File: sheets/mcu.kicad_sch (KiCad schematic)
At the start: 75 parts, among them J11 Conn_01x06, J12 Conn_01x02, J13 USB_B, J14 USB_B, J15 Conn_01x01, J16 Conn_01x01, J8 Conn_02x05_Odd_Even, J9 Conn_01x06, SW1 SW_Push, SW2 SW_Push, U23 REF3333, U24 LPS25HB, U25 XTSD04GLGEAG, U26 STM32H753ZIT6, U27 USBLC6-2SC6, U28 S3225SMD32.768KOSC, Y1 8MHz

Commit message: Remediate power supply, main relay keep-alive, and schematic ERC to 0 errors
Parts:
- removed C106: 100n, Capacitor_SMD:C_0603_1608Metric, symbol Device:C_Small
- removed U28: S3225SMD32.768KOSC, Package_TO_SOT_SMD:SOT-23-5, symbol Regulator_Linear:MIC5205-3.3YM5
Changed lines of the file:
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@@
 	)
 	(symbol
-		(lib_id "power:PWR_FLAG")
-		(at 91.44 247.65 90)
-		(unit 1)
-		(exclude_from_sim no)
-		(in_bom yes)
-		(on_board yes)
-		(dnp no)
-		(property "Reference" "#FLG07"
-			(at 89.535 247.65 0)
-			(effects
-				(font
-					(size 1.27 1.27)
-				)
-				(hide yes)
-			)
-		)
-		(property "Value" "PWR_FLAG"
-			(at 87.0458 247.65 0)
-			(effects
-				(font
-					(size 1.27 1.27)
-				)
-			)
-		)
-		(property "Footprint" ""
-			(at 91.44 247.65 0)
-			(effects
-				(font
-					(size 1.27 1.27)
-				)
-				(hide yes)
-			)
-		)
-		(property "Datasheet" "~"
-			(at 91.44 247.65 0)
-			(effects
-				(font
-					(size 1.27 1.27)
-				)
-				(hide yes)
-			)
-		)
-		(property "Description" ""
-			(at 91.44 247.65 0)
-			(effects
-				(font
-					(size 1.27 1.27)
-				)
-				(hide yes)
-			)
-		)
-		(pin "1"
-		)
-		(instances
-			(project "fome-mc"
-				(path "/3b9c5ffd-e59b-402d-8c5e-052f7ca643a4/00000000-0000-0000-0000-00005d99e6ee"
-					(reference "#FLG07")
-					(unit 1)
-				)
-			)
-		)
-	)
-	(symbol
-		(lib_id "power:PWR_FLAG")
-		(at 100.33 244.475 270)
-		(unit 1)
-		(exclude_from_sim no)
-		(in_bom yes)
-		(on_board yes)
-		(dnp no)
-		(property "Reference" "#FLG08"
-			(at 102.235 244.475 0)
-			(effects
-				(font
-					(size 1.27 1.27)
-				)
-				(hide yes)
-			)
-		)
-		(property "Value" "PWR_FLAG"
-			(at 104.7242 244.475 0)
-			(effects
-				(font
-					(size 1.27 1.27)
-				)
-			)
-		)
-		(property "Footprint" ""
-			(at 100.33 244.475 0)
-			(effects
-				(font
-					(size 1.27 1.27)
-				)
-				(hide yes)
-			)
-		)
-		(property "Datasheet" "~"
-			(at 100.33 244.475 0)
-			(effects
-				(font
-					(size 1.27 1.27)
-				)
-				(hide yes)
-			)
-		)
-		(property "Description" ""
-			(at 100.33 244.475 0)
-			(effects
-				(font
-					(size 1.27 1.27)
-				)
-				(hide yes)
-			)
-		)
-		(pin "1"
-		)
-		(instances
-			(project "fome-mc"
-				(path "/3b9c5ffd-e59b-402d-8c5e-052f7ca643a4/00000000-0000-0000-0000-00005d99e6ee"
-					(reference "#FLG08")
-					(unit 1)
-				)
-			)
-		)
-	)
-	(symbol
 		(lib_id "Connector_Generic:Conn_01x05")
 		(at 329.565 102.235 0)
@@
 		(effects (font (size 1.27 1.27)) (justify left bottom))
 	)
-	(symbol
-		(lib_id "Device:C_Small")
-		(at 235.0 44.45 0)
-		(unit 1)
-		(exclude_from_sim no)
-		(in_bom yes)
-		(on_board yes)
-		(dnp no)
-		(property "Reference" "C106"
-			(at 236.5 43.18 0)
-			(effects (font (size 1.27 1.27)) (justify left))
-		)
-		(property "Value" "100n"
-			(at 236.5 45.720000000000006 0)
-			(effects (font (size 1.27 1.27)) (justify left))
-		)
-		(property "Footprint" "Capacitor_SMD:C_0603_1608Metric"
-			(at 235.0 44.45 0)
-			(effects (font (size 1.27 1.27)) (hide yes))
-		)
-		(property "Datasheet" "~"
-			(at 235.0 44.45 0)
-			(effects (font (size 1.27 1.27)) (hide yes))
-		)
-		(property "LCSC" "C14663"
-			(at 235.0 44.45 0)
-			(effects (font (size 1.27 1.27)) (hide yes))
-		)
-		(pin "1")
-		(pin "2")
-		(instances
-			(project "fome-mc"
-				(path "/3b9c5ffd-e59b-402d-8c5e-052f7ca643a4/00000000-0000-0000-0000-00005d99e6ee"
-					(reference "C106")
-					(unit 1)
-				)
-			)
-		)
-	)
-	(symbol
-		(lib_id "Regulator_Linear:MIC5205-3.3YM5")
-		(at 235.0 34.29 0)
-		(unit 1)
-		(exclude_from_sim no)
-		(in_bom yes)
-		(on_board yes)
-		(dnp no)
-		(property "Reference" "U28"
-			(at 235.0 29.21 0)
-			(effects (font (size 1.27 1.27)))
-		)
-		(property "Value" "S3225SMD32.768KOSC"
-			(at 235.0 39.37 0)
-			(effects (font (size 1.27 1.27)))
-		)
-		(property "Footprint" "Package_TO_SOT_SMD:SOT-23-5"
-			(at 235.0 34.29 0)
-			(effects (font (size 1.27 1.27)) (hide yes))
-		)
-		(property "Datasheet" "~"
-			(at 235.0 34.29 0)
-			(effects (font (size 1.27 1.27)) (hide yes))
-		)
-		(property "LCSC" "C7431189"
-			(at 235.0 34.29 0)
-			(effects (font (size 1.27 1.27)) (hide yes))
-		)
-		(pin "1")
-		(pin "2")
-		(pin "3")
-		(pin "4")
-		(pin "5")
-		(instances
-			(project "fome-mc"
-				(path "/3b9c5ffd-e59b-402d-8c5e-052f7ca643a4/00000000-0000-0000-0000-00005d99e6ee"
-					(reference "U28")
-					(unit 1)
-				)
-			)
-		)
-	)
 	(hierarchical_label "BOOT0"

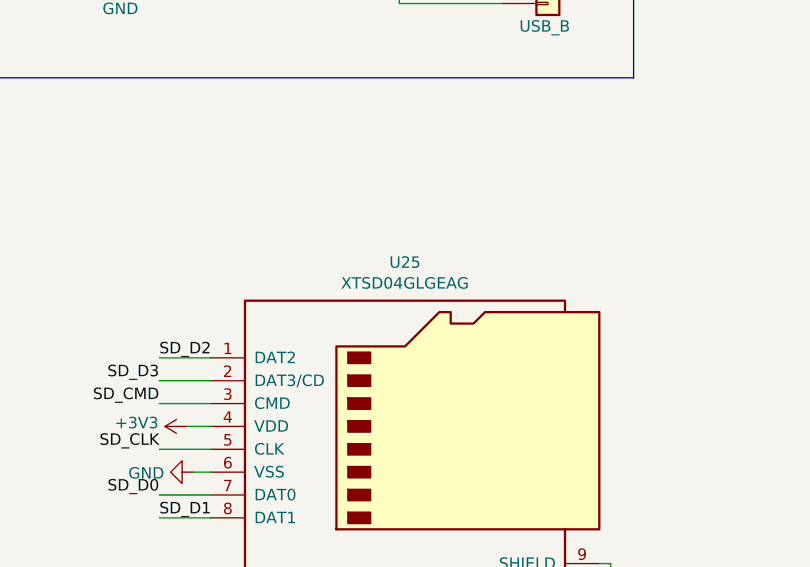
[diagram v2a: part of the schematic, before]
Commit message: FOMEMC-3: Upgrade U25 soldered SDNAND from 512 MB (4 Gbit) to 4 GB (32 Gbit CSNP32GCR01-AOW)
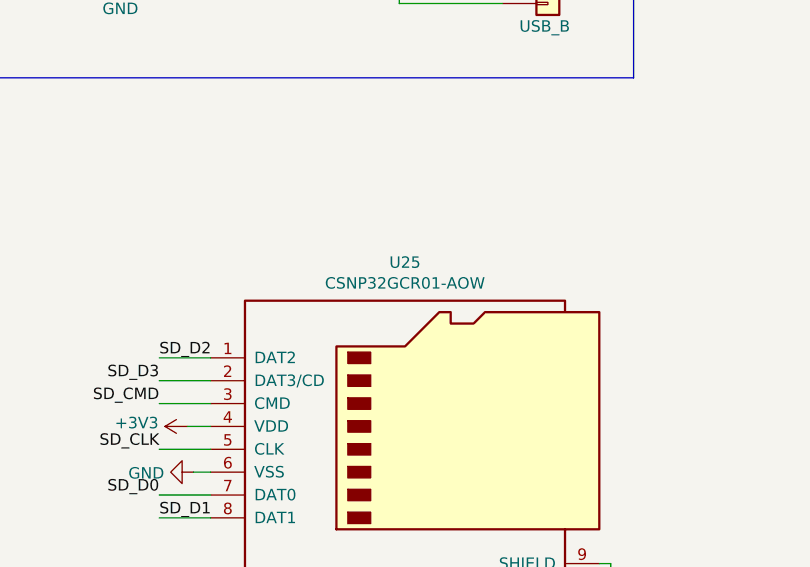
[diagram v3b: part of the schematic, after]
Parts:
- U25: value XTSD04GLGEAG -> CSNP32GCR01-AOW; LCSC C558840 -> C2841139; PN XTSD04GLGEAG -> CSNP32GCR01-AOW
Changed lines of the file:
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@@
 			)
 		)
-		(property "Value" "XTSD04GLGEAG"
+		(property "Value" "CSNP32GCR01-AOW"
 			(at 313.69 156.1846 0)
 			(effects
@@
 			)
 		)
-		(property "Datasheet" "https://datasheet.lcsc.com/lcsc/2005251034_XTX-XTSD04GLGEAG_C558840.pdf"
+		(property "Datasheet" "https://datasheet.lcsc.com/lcsc/2204261630_CS-CSNP32GCR01-AOW_C2841139.pdf"
 			(at 314.96 172.085 0)
 			(effects
@@
 			)
 		)
-		(property "Description" "4Gbit (512MB) Soldered Pottable SD NAND Flash LGA-8 6x8mm"
+		(property "Description" "32Gbit (4GB) Soldered Pottable SD NAND Flash LGA-8 6x8mm"
 			(at 314.96 172.085 0)
 			(effects
@@
 			)
 		)
-		(property "LCSC" "C558840"
+		(property "LCSC" "C2841139"
 			(at 314.96 172.085 0)
 			(effects
@@
 			)
 		)
-		(property "PN" "XTSD04GLGEAG"
+		(property "PN" "CSNP32GCR01-AOW"
 			(at 314.96 172.085 0)
 			(effects
@@
 			(project "fome-mc"
 				(path "/3b9c5ffd-e59b-402d-8c5e-052f7ca643a4/00000000-0000-0000-0000-00005d99e6ee"
-					(reference "U25")
-					(unit 1)
-				)
-			)
-			(project "fome-mc"
-				(path "/3b9c5ffd-e59b-402d-8c5e-052f7ca643a4/00000000-0000-0000-0000-00005d99e6ee"

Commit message: Re-integrate ATWINC1500-MR210UB Wi-Fi on SPI4 and remap WBO1/2 reset/boot pins (FOMEMC-2)
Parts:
- added C106: 100n, Capacitor_SMD:C_0603_1608Metric, symbol Device:C_Small
- added R122: 10k, Resistor_SMD:R_0402_1005Metric, symbol Device:R_Small
- added U29: ATWINC1500-MR210UB, ampseal:ATWINC1500-MR210UB, symbol RF_WiFi:ATWINC1500-MR210UB
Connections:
- net IGN12 is gone; now on net WBO1_NRST: U26.118 (PD4)
- net IGN9 is gone; now on net WBO2_BOOT0: U26.123 (PD7)
- net +3V3: now also C106.1, R122.1, U29.20 (VBAT), U29.23 (VDDIO)
- net GND: now also C106.2, U29.12 (GND_2), U29.28 (GND_3), U29.29 (EP), U29.9 (GND_1)
- net WBO1_BOOT0: now also U26.119 (PD5); no longer U26.2 (PE3)
- net WBO1_NRST: no longer U26.1 (PE2)
- net WBO2_BOOT0: no longer U26.4 (PE5)
- net WBO2_NRST: now also U26.122 (PD6); no longer U26.3 (PE4)
- net WIFI_MOSI: now reaches U26.5 (PE6)
- net WIFI_MOSI: now also U29.15 (SPI_RXD)
- net WIFI_RST: now reaches U26.7 (PC13)
- net WIFI_RST: now also U29.4 (RESET_N)
- net IGN10: no longer names the net of J12.2 (Pin_2)
- net IGN10: no longer U26.122 (PD6)
- net IGN11: no longer names the net of J12.1 (Pin_1)
- net IGN11: no longer U26.119 (PD5)
- new net WIFI_CS: U26.3 (PE4), U29.16 (SPI_SSN)
- new net WIFI_EN: R122.2, U29.10 (SPI_CFG), U29.11 (WAKE), U29.22 (CHIP_EN)
- new net WIFI_IRQ: U26.2 (PE3), U29.13 (IRQN)
- new net WIFI_MISO: U26.4 (PE5), U29.17 (SPI_TXD)
- new net WIFI_SCK: U26.1 (PE2), U29.18 (SPI_SCK)
- no-connect marks 18 -> 32

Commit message: Add SDMMC1 47k pull-ups (R127..R131) & 22R clock damping (R132), mark U24 LPS25HB DNP, fix B340A/B5819W LCSC codes, and reconcile docs/verify_io_map (FOMEMC-8)
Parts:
- added R127, R128, R129, R130, R131: 47k, Resistor_SMD:R_0402_1005Metric, symbol Device:R
- added R132: 22, Resistor_SMD:R_0603_1608Metric, symbol Device:R
- D14, D6, D7, D8: value schottky -> B5819W
- U24: now not fitted; now left out of the parts list
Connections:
- net +3V3: now also R127.1, R128.1, R129.1, R130.1, R131.1
- net SD_CLK: now also R132.1; no longer U25.5 (CLK)
- net SD_CMD: now also R131.2
- net SD_D0: now also R127.2
- net SD_D1: now also R128.2
- net SD_D2: now also R129.2
- net SD_D3: now also R130.2
- new net: R132.2, U25.5 (CLK)

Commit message: Synchronize PCB footprints, netlist pad assignments, DNP flags, and zone priorities with schematic (FOMEMC-9)
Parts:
- D10, D11, D12, D13, D9: footprint LED_SMD:LED_0603_1608Metric_Castellated -> LED_SMD:LED_0603_1608Metric
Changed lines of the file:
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@@
 			)
 		)
-		(property "Footprint" "LED_SMD:LED_0603_1608Metric_Castellated"
+		(property "Footprint" "LED_SMD:LED_0603_1608Metric"
 			(at 211.455 173.99 0)
 			(effects
@@
 			)
 		)
-		(property "Footprint" "LED_SMD:LED_0603_1608Metric_Castellated"
+		(property "Footprint" "LED_SMD:LED_0603_1608Metric"
 			(at 211.455 184.15 0)
 			(effects
@@
 			)
 		)
-		(property "Footprint" "LED_SMD:LED_0603_1608Metric_Castellated"
+		(property "Footprint" "LED_SMD:LED_0603_1608Metric"
 			(at 211.455 193.675 0)
 			(effects
@@
 			)
 		)
-		(property "Footprint" "LED_SMD:LED_0603_1608Metric_Castellated"
+		(property "Footprint" "LED_SMD:LED_0603_1608Metric"
 			(at 211.455 203.2 0)
 			(effects
@@
 			)
 		)
-		(property "Footprint" "LED_SMD:LED_0603_1608Metric_Castellated"
+		(property "Footprint" "LED_SMD:LED_0603_1608Metric"
 			(at 211.455 212.725 0)
 			(effects

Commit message: Remediate FOMEMC-17..20: 50V X7R PSU caps & 42V INJ clamp DNP, U29 DS70005304F footprint + 1P3V bypass, HV_IGN 0.50mm clearance + U25 decoupling, and 0 ERC violations
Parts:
- added C111: 10u, Capacitor_SMD:C_0603_1608Metric, symbol Device:C_Small
- added C112: 10n, Capacitor_SMD:C_0603_1608Metric, symbol Device:C_Small
- added C113: 4.7u, Capacitor_SMD:C_0603_1608Metric, symbol Device:C_Small
- added C114: 100n, Capacitor_SMD:C_0603_1608Metric, symbol Device:C_Small
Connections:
- net +3V3: now also C113.1, C114.1
- net GND: now also C111.2, C112.2, C113.2, C114.2
- net WIFI_1P3V: now reaches U29.24 (1P3V_TP)
- net WIFI_1P3V: now also C111.1, C112.1
- net LS10: no longer names the net of U26.135 (PB5)
- net LS11: no longer names the net of U26.136 (PB6)
- net LSE_32K: no longer names the net of U26.8 (PC14)
- net RC1: no longer names the net of U26.100 (PA8)
- net TRIGGER_SCOPE: no longer names the net of U26.22 (PF10)
- no-connect marks 32 -> 36

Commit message: Remediate FOMEMC-22..27: sheet contracts, doc/BOM/netlist parity, 494-part BOM/CPL, Mode A2 VR + C38/C39, wide WBO heater buses, and 4x M4 holes with 0 DRC warnings
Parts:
- BT1, J11, J12, J13, J14, J15, J16, J8, J9: now not fitted; now left out of the parts list
- C103, C104, C105, C106, C114, C61, C62, C63, C64, C67, C68, C69, C70, C71, C73, C79, C81, C83: LCSC C14663 -> C161115
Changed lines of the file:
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@@
 			)
 		)
-		(property "LCSC" "C14663"
+		(property "LCSC" "C161115"
 			(at 43.18 29.845 0)
 			(effects
@@
 			)
 		)
-		(property "LCSC" "C14663"
+		(property "LCSC" "C161115"
 			(at 48.26 29.845 0)
 			(effects
@@
 			)
 		)
-		(property "LCSC" "C14663"
+		(property "LCSC" "C161115"
 			(at 53.34 29.845 0)
 			(effects
@@
 			)
 		)
-		(property "LCSC" "C14663"
+		(property "LCSC" "C161115"
 			(at 58.42 29.845 0)
 			(effects
@@
 			)
 		)
-		(property "LCSC" "C14663"
+		(property "LCSC" "C161115"
 			(at 68.58 29.845 0)
 			(effects
@@
 			)
 		)
-		(property "LCSC" "C14663"
+		(property "LCSC" "C161115"
 			(at 160.655 57.15 0)
 			(effects
@@
 			)
 		)
-		(property "LCSC" "C14663"
+		(property "LCSC" "C161115"
 			(at 17.78 29.845 0)
 			(effects
@@
 			)
 		)
-		(property "LCSC" "C14663"
+		(property "LCSC" "C161115"
 			(at 22.86 29.845 0)
 			(effects
@@
 			)
 		)
-		(property "LCSC" "C14663"
+		(property "LCSC" "C161115"
 			(at 27.94 29.845 0)
 			(effects
@@
 			)
 		)
-		(property "LCSC" "C14663"
+		(property "LCSC" "C161115"
 			(at 55.88 90.805 0)
 			(effects
@@
 			)
 		)
-		(property "LCSC" "C14663"
+		(property "LCSC" "C161115"
 			(at 95.885 71.12 0)
 			(effects
@@
 		(unit 1)
 		(exclude_from_sim no)
-		(in_bom yes)
+		(in_bom no)
 		(on_board yes)
-		(dnp no)
+		(dnp yes)
 		(property "Reference" "J8"
 			(at 210.82 44.0182 0)
@@
 			)
 		)
-		(property "LCSC" "C14663"
+		(property "LCSC" "C161115"
 			(at 292.735 93.98 0)
 			(effects
@@
 		(unit 1)
 		(exclude_from_sim no)
-		(in_bom yes)
+		(in_bom no)
 		(on_board yes)
-		(dnp no)
+		(dnp yes)
 		(property "Reference" "J13"
 			(at 331.597 101.1682 0)
@@
 		(unit 1)
 		(exclude_from_sim no)
-		(in_bom yes)
+		(in_bom no)
 		(on_board yes)
-		(dnp no)
+		(dnp yes)
 		(property "Reference" "J14"
 			(at 331.597 118.9482 0)
@@
 		(unit 1)
 		(exclude_from_sim no)
-		(in_bom yes)
+		(in_bom no)
 		(on_board yes)
-		(dnp no)
+		(dnp yes)
 		(property "Reference" "J11"
 			(at 317.627 224.3582 0)
@@
 		(unit 1)
 		(exclude_from_sim no)
-		(in_bom yes)
+		(in_bom no)
 		(on_board yes)
-		(dnp no)
+		(dnp yes)
 		(property "Reference" "J12"
 			(at 317.627 244.0432 0)
@@
 		(unit 1)
 		(exclude_from_sim no)
-		(in_bom yes)
+		(in_bom no)
 		(on_board yes)
-		(dnp no)
+		(dnp yes)
 		(property "Reference" "J9"
 			(at 215.392 81.4832 0)
@@
 			)
 		)
-		(property "LCSC" "C14663"
+		(property "LCSC" "C161115"
 			(at 22.86 248.285 0)
 			(effects
@@
 		(unit 1)
 		(exclude_from_sim no)
-		(in_bom yes)
+		(in_bom no)
 		(on_board yes)
-		(dnp no)
+		(dnp yes)
 		(property "Reference" "BT1"
 			(at 90.17 43.053 90)
@@
 		(unit 1)
 		(exclude_from_sim no)
-		(in_bom yes)
+		(in_bom no)
 		(on_board yes)
-		(dnp no)
+		(dnp yes)
 		(fields_autoplaced yes)
 		(property "Reference" "J16"
@@
 		(unit 1)
 		(exclude_from_sim no)
-		(in_bom yes)
+		(in_bom no)
 		(on_board yes)
-		(dnp no)
+		(dnp yes)
 		(fields_autoplaced yes)
 		(property "Reference" "J15"
@@
 			(effects (font (size 1.27 1.27)) (hide yes))
 		)
-		(property "LCSC" "C14663"
+		(property "LCSC" "C161115"
 			(at 255.08 44.45 0)
 			(effects (font (size 1.27 1.27)) (hide yes))
@@
 			(effects (font (size 1.27 1.27)) (hide yes))
 		)
-		(property "LCSC" "C14663"
+		(property "LCSC" "C161115"
 			(at 270.08 44.45 0)
 			(effects (font (size 1.27 1.27)) (hide yes))
@@
 			(effects (font (size 1.27 1.27)) (hide yes))
 		)
-		(property "LCSC" "C14663"
+		(property "LCSC" "C161115"
 			(at 285.08 44.45 0)
 			(effects (font (size 1.27 1.27)) (hide yes))
@@
 			(effects (font (size 1.27 1.27)) (hide yes))
 		)
-		(property "LCSC" "C14663"
+		(property "LCSC" "C161115"
 			(at 335.28 195.58 0)
 			(effects (font (size 1.27 1.27)) (hide yes))
@@
 			(effects (font (size 1.27 1.27)) (hide yes))
 		)
-		(property "LCSC" "C14663"
+		(property "LCSC" "C161115"
 			(at 297.18 208.28 0)
 			(effects (font (size 1.27 1.27)) (hide yes))
